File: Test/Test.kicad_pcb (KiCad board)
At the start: 2 copper layers, 43 x 65 mm, 4 parts, among them J1 Conn_01x20, J2 Conn_01x20, J3 Conn_01x03, U1 Pico

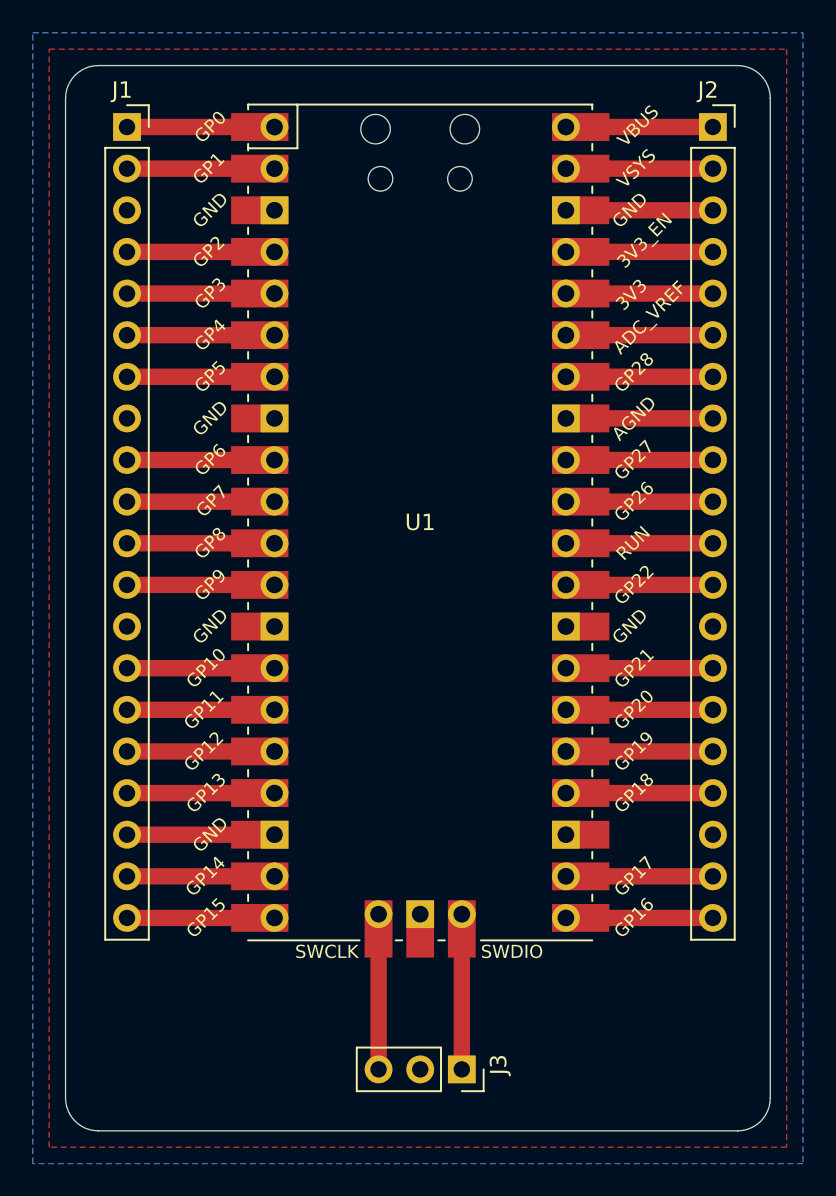
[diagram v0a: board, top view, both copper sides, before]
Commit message: Update to KiCad 6
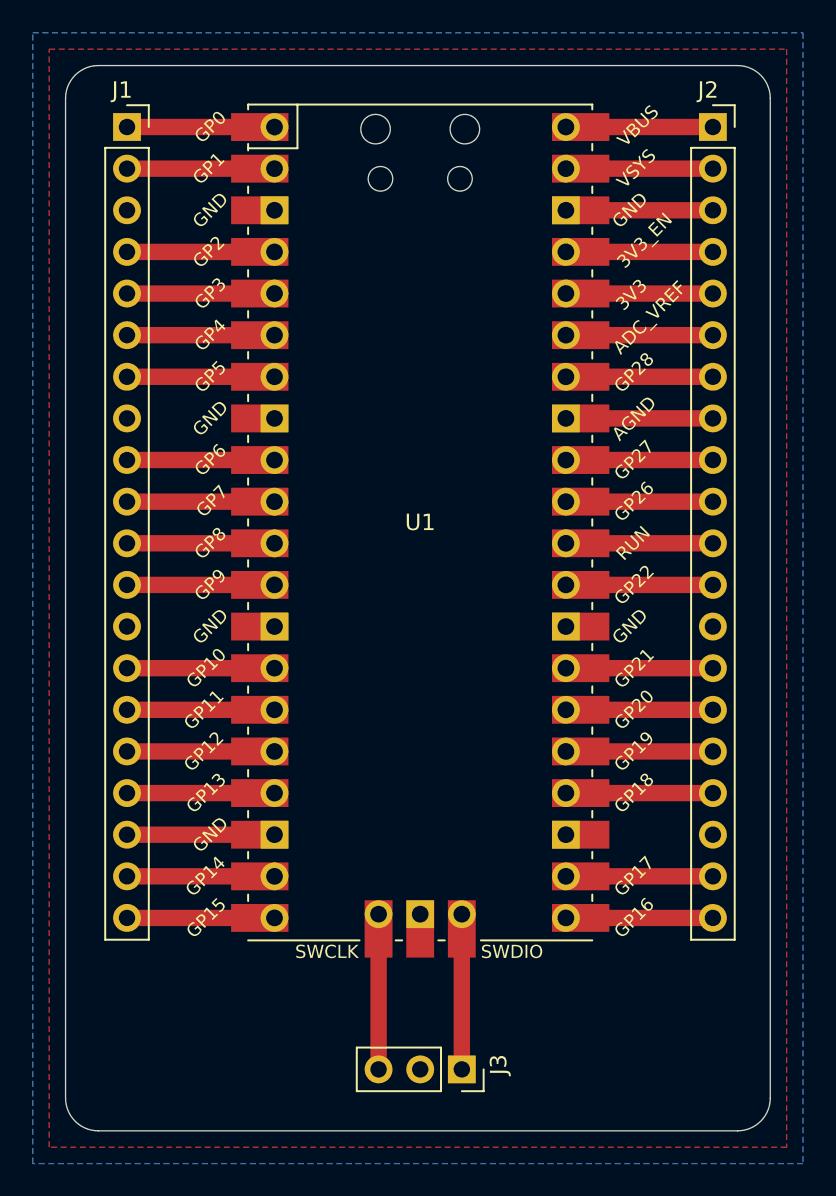
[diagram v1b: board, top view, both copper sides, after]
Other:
- net class Default removed
